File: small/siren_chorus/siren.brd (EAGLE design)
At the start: 33 x 53.3 mm, 50 parts, among them IC1 NE5532, IC2 PT2399, Q1 2N5457

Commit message: formatting updates
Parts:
- C1: value 100uF -> 100u
- C10, C11, C16, C17, C2, C9: value 0.1uF -> 100n
- C12: value 0.1uF -> 3n3
- C13: value 0.1uF -> 10n
- C14: value 10nF -> 100n
- C15: value 3.3nF -> 100n
- C3: value 0.01uF -> 10n
- C4: value 47uF -> 47u
- C5: value 10uF -> 47u
- C6: value 47uF -> 10u
- C7: value 10uF -> 10u
- C8: value 3.9nF -> 3n9
- R1: value 220k -> 1M
- R3: value 1M -> 220k
- RATE: value 100k -> 100kB
- moved PAD2 47.6 mm to (26.7, 50.2), turned to 180 degrees
- moved PAD1 46.4 mm to (24.1, 3.17), turned to 0 degrees
- moved R3 29.7 mm to (15.2, 35.6)
- moved R1 25.0 mm to (25.4, 12.7), turned to 270 degrees
- moved C12 20.9 mm to (15.2, 22.9), turned to 270 degrees
- moved C15 20.9 mm to (10.2, 2.54), turned to 0 degrees
- moved R10 17.8 mm to (10.2, 27.9), turned to 0 degrees
- moved R11 17.8 mm to (27.9, 27.9), turned to 180 degrees
- moved R18 7.62 mm to (17.8, 17.8)
- moved R20 7.62 mm to (17.8, 10.2)
- moved C13 7.62 mm to (17.8, 15.2), turned to 0 degrees
- moved C14 7.62 mm to (17.8, 7.62), turned to 180 degrees
- moved C10 7.62 mm to (2.54, 5.08)
- moved C9 7.62 mm to (2.54, 12.7)
- moved R5 5.68 mm to (25.4, 40.6), turned to 0 degrees
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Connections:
- removed net N$27: C3.1, IC1.1, R5.1, R9.2
- new net N$30: C3.1, IC1.1, R6.1, R9.2
- net +9V: now also PAD2.1; no longer PAD1.1
- net GND: now also R10.1; no longer R11.1
- net IN: now also PAD1.1, R1.2; no longer PAD2.1, R3.2
- net N$1: now also C12.1; no longer C15.1
- net N$10: now also C15.1; no longer C12.1
- net N$11: now also C15.2; no longer C12.2
- net N$14: now also R11.1; no longer R10.1
- net N$15: now also R11.2; no longer R10.2
- net N$18: now also C5.+; no longer C6.+
- net N$2: now also C12.2; no longer C15.2
- net N$23: now also C9.1; no longer C10.1
- net N$24: now also C10.1; no longer C9.1
- net N$25: now also R3.2, R6.2; no longer R1.2, R5.2
- net N$26: now also R5.2; no longer R6.2
- net N$28: now also C6.+, R5.1; no longer C5.+, R6.1
- net N$31: now also R10.2; no longer R11.2
- net N$5: now also C13.1, R18.2; no longer C14.1, R20.2
- net N$6: now also C14.1, R20.2; no longer C13.1, R18.2
- net N$7: now also C13.2; no longer C14.2
- net N$9: now also C14.2; no longer C13.2
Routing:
- net N$30: track 0.00 -> 8.67 mm
- net N$27: track 8.67 -> 0.00 mm
- net IN: track 7.62 -> 11.8 mm
- net OUT: track 17.0 -> 16.4 mm

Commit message: add beginnings of tremolo; minor copy tweaks to other schems
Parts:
- Q1: value 2N5457 -> J112
- R12: value 2.2k -> 2k2
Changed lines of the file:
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@@
 <element name="DEPTH" library="potentiometers" package="2262_TRIM" value="500k" x="5.08" y="49.53" rot="R180"/>
 <element name="RATE" library="potentiometers" package="PADS_SMALL" value="100kB" x="13.335" y="50.8"/>
-<element name="Q1" library="transistors" package="TO92-" value="2N5457" x="10.16" y="25.4"/>
+<element name="Q1" library="transistors" package="TO92-" value="J112" x="10.16" y="25.4"/>
 <element name="R1" library="resistors" package="R0207/2V" value="1M" x="25.4" y="12.7" rot="R270"/>
 <element name="R13" library="resistors" package="R0207/2V" value="10k" x="22.86" y="25.4" rot="R90"/>
@@
 <element name="R20" library="resistors" package="R0207/2V" value="10k" x="17.78" y="10.16" rot="R180"/>
 <element name="R19" library="resistors" package="R0207/2V" value="10k" x="17.78" y="12.7" rot="R180"/>
-<element name="R12" library="resistors" package="R0207/2V" value="2.2k" x="2.54" y="20.32" rot="R90"/>
+<element name="R12" library="resistors" package="R0207/2V" value="2k2" x="2.54" y="20.32" rot="R90"/>
 <element name="R2" library="resistors" package="R0207/2V" value="220k" x="21.59" y="48.26" rot="R180"/>
 <element name="R3" library="resistors" package="R0207/2V" value="220k" x="15.24" y="35.56"/>

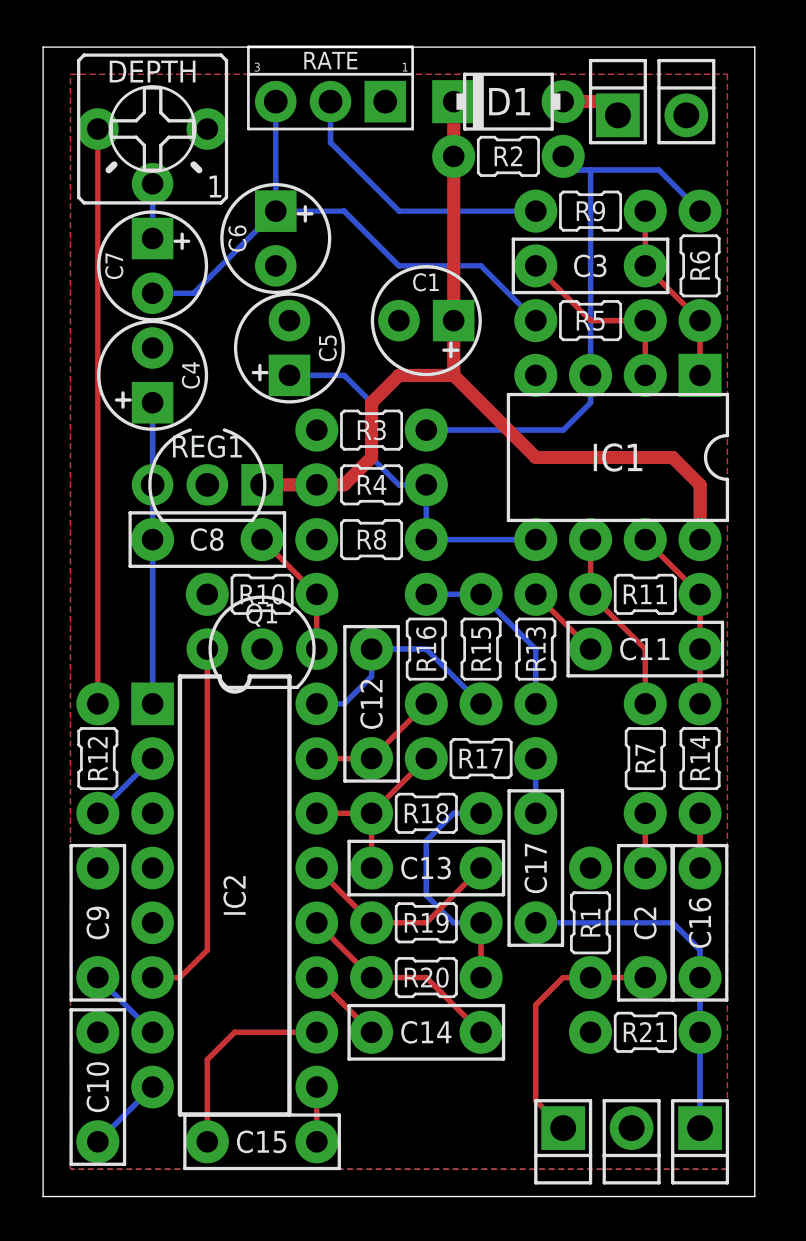
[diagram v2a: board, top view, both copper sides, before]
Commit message: add EAGLE library, update 1590a chorus and tremolo, other minor edits
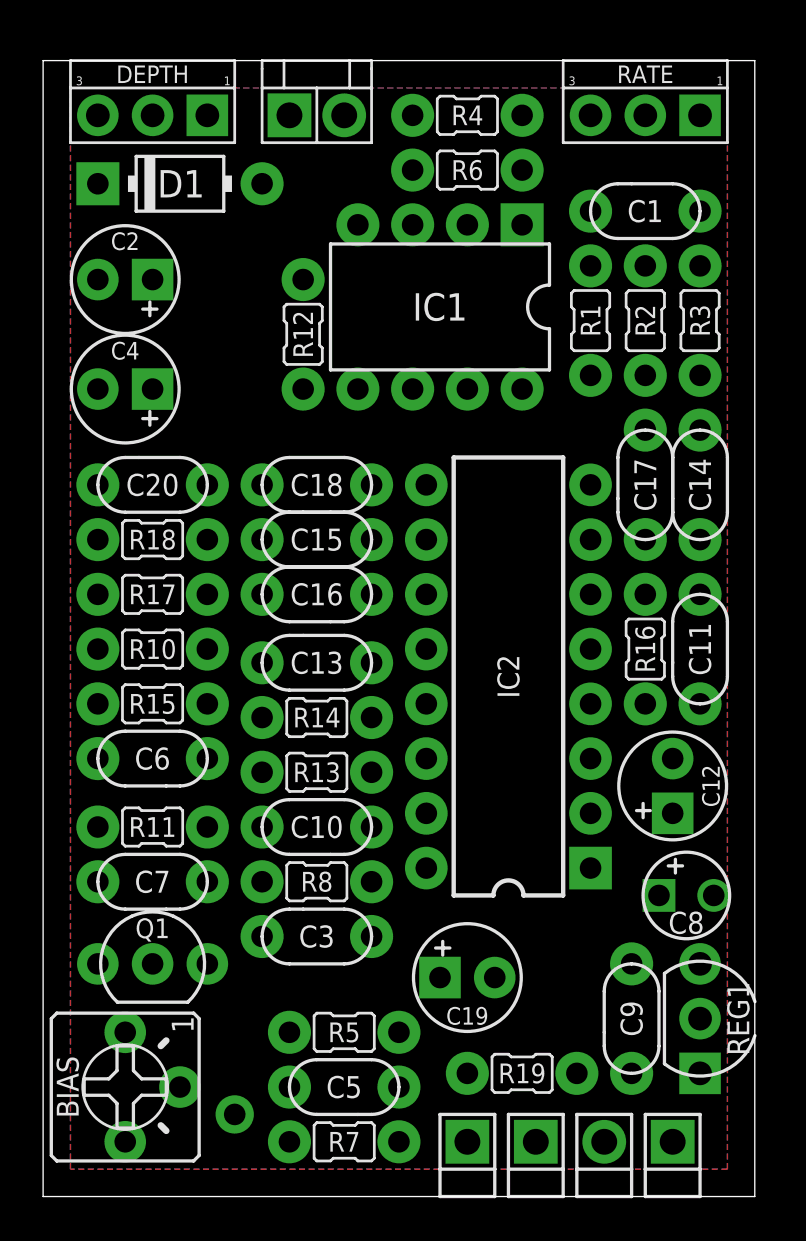
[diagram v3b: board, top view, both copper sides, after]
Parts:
- removed PAD1, PAD5: PADSQR, supply pins:SQUARE
- removed PAD3, PAD4: PADRND, supply pins:ROUND
- removed R20: 10k, resistors:R0207/2V
- removed R21: 100k, resistors:R0207/2V
- removed R9: 4k7, resistors:R0207/2V
- added 9V: DC_MONO, jacks:DC
- added BIAS: 50k, potentiometers:2262_TRIM
- added C18: 100n, capacitors-film:050X030_025_2
- added C19: 4u7, capacitors-elec:050_020_1
- added C20: 10n, capacitors-film:050X030_025_2
- added GND: PADRND, supply pins:ROUND
- added IN, LED, OUT: PADSQR, supply pins:SQUARE
- C1: value 100u -> 10n; device capacitors-elec:050_020_1 -> capacitors-film:050X030_025_2
- C10: value 100n -> 2n2; device capacitors-film:BOX_SMALL -> capacitors-film:050X030_025_2
- C11: value 100n -> 10n; device capacitors-film:BOX_SMALL -> capacitors-film:050X030_025_2
- C12: value 3n3 -> 10u; device capacitors-film:BOX_SMALL -> capacitors-elec:050_020_1
- C13: value 10n -> 100p; device capacitors-film:BOX_SMALL -> capacitors-film:050X030_025_2
- C14, C15, C17, C9: device capacitors-film:BOX_SMALL -> capacitors-film:050X030_025_2
- C16: value 100n -> 220n; device capacitors-film:BOX_SMALL -> capacitors-film:050X030_025_2
- C2: value 100n -> 47u; device capacitors-film:BOX_SMALL -> capacitors-elec:050_020_1
- C3: value 10n -> 100n; device capacitors-film:BOX_SMALL -> capacitors-film:050X030_025_2
- C4: value 47u -> 10u
- C5: value 47u -> 10n; device capacitors-elec:050_020_1 -> capacitors-film:050X030_025_2
- C6: value 10u -> 22n; device capacitors-elec:050_020_1 -> capacitors-film:050X030_025_2
- C7: value 10u -> 220n; device capacitors-elec:050_020_1 -> capacitors-film:050X030_025_2
- C8: value 3n9 -> 10u; device capacitors-film:BOX_SMALL -> capacitors-elec:050_020
- D1: value 1N5817 -> 1N4817; device diodes:DO41-2 -> diodes:DO41-3
- DEPTH: value 500k -> 10kB; device potentiometers:2262_TRIM -> potentiometers:PADS_SMALL
- IC2: value PT2399 -> (none)
- PAD2: value PADSQR -> PAD; device supply pins:SQUARE -> supply pins:UNLABELED
- Q1: value J112 -> 2N5457
- R1: value 1M -> 100k
- R10: value 1M -> 18k
- R11: value 1M -> 10k
- R12: value 2k2 -> 18k
- R14: value 10k -> 18k
- R16: value 10k -> 2k
- R17: value 10k -> 12k
- R18: value 10k -> 4k7
- R2: value 220k -> 100k
- R4: value 10k -> 220k
- R5: value 220k -> 1M
- R6: value 220k -> 15k
- R7: value 470k -> 1M
- RATE: value 100kB -> 100kC
- moved PAD2 49.6 mm to (8.89, 3.81), turned to 0 degrees
- moved C2 38.4 mm to (3.81, 42.5), turned to 180 degrees
- moved R5 34.9 mm to (14.0, 7.62)
- moved C5 34.4 mm to (14.0, 5.08), turned to 0 degrees
- moved REG1 33.7 mm to (30.5, 8.26), turned to 90 degrees
- moved C3 33.6 mm to (12.7, 12.1)
- moved C7 28.6 mm to (5.08, 14.6), turned to 0 degrees
- moved C14 28.4 mm to (30.5, 33.0), turned to 270 degrees
- moved C15 28.1 mm to (12.7, 30.5), turned to 180 degrees
- moved R1 27.9 mm to (25.4, 40.6)
- moved C8 27.7 mm to (29.8, 14.0)
- moved R11 25.3 mm to (5.08, 17.1), turned to 0 degrees
- moved C9 25.2 mm to (27.3, 8.26), turned to 270 degrees
- moved C6 24.8 mm to (5.08, 20.3), turned to 0 degrees
- moved C16 23.4 mm to (12.7, 27.9), turned to 0 degrees
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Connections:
- removed net N$1: C12.1, IC2.16, R15.1
- removed net N$2: C12.2, IC2.15, R16.1
- removed net N$29: R9.1, RATE.2
- removed net N$30: C3.1, IC1.1, R6.1, R9.2
- removed net N$32: C1.+, D1.C, IC1.8, R2.2, R4.1, REG1.1
- new net LED: DEPTH.3, IC1.6, IC1.7, LED.1
- new net N$27: R6.1, RATE.3
- new net VC: BIAS.1, C2.+, C3.1, D1.C, IC1.8, R1.2, REG1.1
- net +9V: now also 9V.T; no longer PAD2.1
- net GND: now also 9V.S, C11.2, C12.-, C14.2, C17.2, C2.-, C20.1, C3.2, C8.-, DEPTH.1, GND.1, R16.1, R19.1, R2.1, R5.1, R7.1; no longer C1.-, C10.2, C5.-, C6.-, PAD3.1, PAD4.1, Q1.2, R1.1, R10.1, R21.1, R3.1
- net IN: now also C5.2, IN.1, R5.2; no longer C2.2, PAD1.1, R1.2
- net N$10: now also IC2.11; no longer IC2.10
- net N$11: now also C18.2, IC2.10; no longer C15.2, IC2.9
- net N$12: now also C18.1, IC2.9; no longer C17.2, R17.2
- net N$13: now also C13.2, C19.+, IC2.14, R15.1; no longer C16.2, R14.1
- net N$14: now also C13.1, IC2.13, R10.2, R15.2, R17.1; no longer C11.1, IC1.7, R11.1, R14.2
- net N$15: now also R13.2, R14.2; no longer IC1.6, R7.1
- net N$16: now also C7.1, R11.1; no longer C2.1, R7.2
- net N$17: now also C7.2, Q1.2, R8.2; no longer C11.2, R13.2
- net N$18: now also C6.1, R10.1; no longer C5.+, IC1.5, R4.2, R8.2
- net N$19: now also BIAS.2, BIAS.3, C6.2, PAD2.P$1, Q1.3; no longer C4.+, C8.1, IC2.1, REG1.3
- net N$20: now also C5.1, Q1.1, R7.2; no longer IC2.2, R12.1
- net N$21: now also IC1.3, R1.1, R2.2, R3.1; no longer IC2.6, Q1.3
- net N$22: now also C15.2, C16.2, IC2.12; no longer C7.+, DEPTH.2
- net N$23: now also C16.1, R18.1; no longer C9.1, IC2.7
- net N$24: now also C1.1, IC1.1, R3.2, RATE.1, RATE.2; no longer C10.1, IC2.8
- net N$25: now also C1.2, IC1.2, R4.1; no longer IC1.3, R2.1, R3.2, R6.2
- net N$26: now also DEPTH.2, R12.1; no longer C3.2, IC1.2, R5.2
- net N$28: now also C4.+, IC1.5, R4.2, R6.2; no longer C6.+, C7.-, R5.1, RATE.3
- net N$3: now also C8.+, C9.1, IC2.1, REG1.3; no longer DEPTH.3, R12.2
- net N$31: now also C11.1, IC2.6, R12.2, R16.2; no longer C8.2, Q1.1, R10.2
- net N$4: now also C10.2, IC2.16; no longer R15.2, R16.2
- net N$5: now also C10.1, IC2.15, R14.1; no longer C13.1, IC2.14, R17.1, R18.2
- net N$6: now also C20.2, R17.2, R18.2; no longer C14.1, IC2.12, R20.2
- net N$7: now also C12.+, IC2.2; no longer C13.2, IC2.13, R19.2
- net N$8: now also C14.1, IC2.7; no longer R18.1, R19.1, R20.1
- net N$9: now also C17.1, IC2.8; no longer C14.2, IC2.11
- net OUT: now also C19.-, OUT.1, R19.2; no longer C16.1, C17.1, PAD5.1, R21.2
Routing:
- net N$32: track 41.3 -> 0.00 mm
- net N$3: track 26.7 -> 0.00 mm
- net N$28: track 26.5 -> 0.00 mm
- net N$25: track 26.3 -> 0.00 mm
- net N$18: track 17.6 -> 0.00 mm
- net N$21: track 17.0 -> 0.00 mm
- net OUT: track 16.4 -> 0.00 mm
- net N$19: track 14.0 -> 0.00 mm
- net N$29: track 12.7 -> 0.00 mm
- net IN: track 11.8 -> 0.00 mm
- net N$8: track 11.2 -> 0.00 mm
- net N$1: track 10.5 -> 0.00 mm
- net N$7: track 9.72 -> 0.00 mm
- net N$6: track 9.72 -> 0.00 mm
- net N$10: track 9.42 -> 0.00 mm
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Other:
- board size 33 x 53.3 mm -> 33 x 52.7 mm
